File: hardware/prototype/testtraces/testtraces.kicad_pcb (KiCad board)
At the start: 2 copper layers, 0 parts

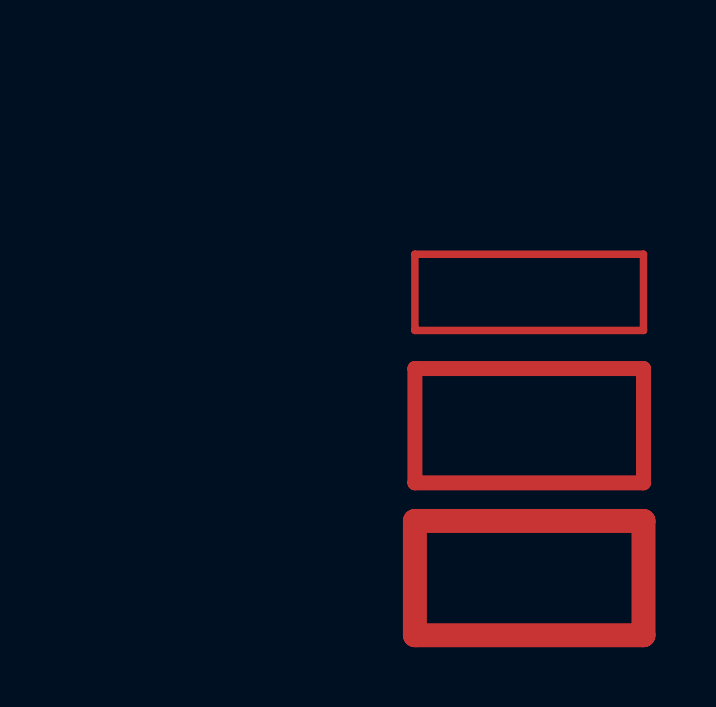
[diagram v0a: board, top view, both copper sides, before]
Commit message: Rerouted pi connect prototype for a slightly smaller board.
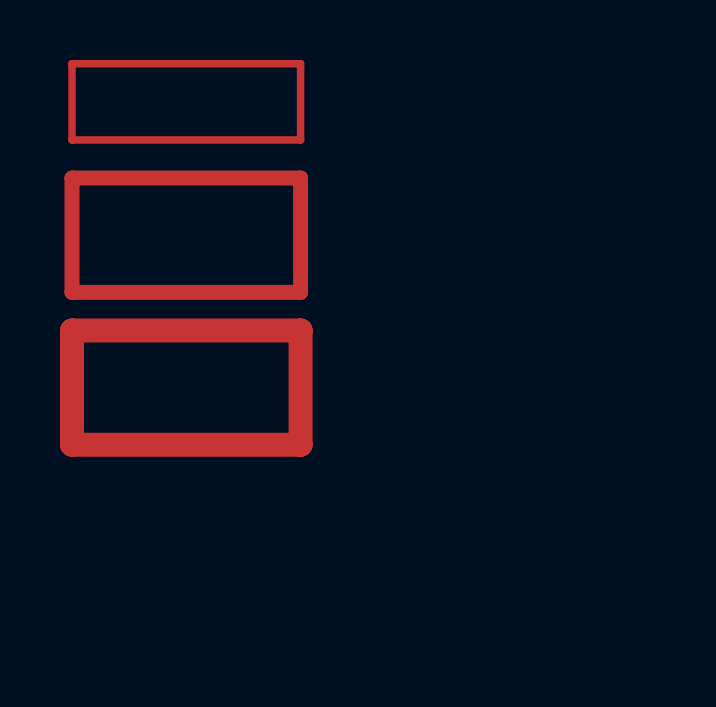
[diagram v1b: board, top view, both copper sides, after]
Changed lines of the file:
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@@
     (uvia_drill 0.1)
   )
-  (gr_text "0.6\n" (at 36.83 29.21) (layer Dwgs.User)
+  (gr_text "0.6\n" (at 25.4 22.86) (layer Dwgs.User)
     (effects (font (size 1.5 1.5) (thickness 0.3)))
   )
-  (gr_text 0.5 (at 36.83 25.4) (layer Dwgs.User)
+  (gr_text 0.5 (at 25.4 19.05) (layer Dwgs.User)
     (effects (font (size 1.5 1.5) (thickness 0.3)))
   )
-  (gr_text 0.25 (at 34.29 20.32) (layer Dwgs.User)
+  (gr_text 0.25 (at 22.86 13.97) (layer Dwgs.User)
     (effects (font (size 1.5 1.5) (thickness 0.3)) (justify left))
   )
-  (segment (start 31.75 21.59) (end 24.13 21.59) (width 0.25) (layer F.Cu) (net 0))
-  (segment (start 31.75 19.05) (end 31.75 21.59) (width 0.25) (layer F.Cu) (net 0))
-  (segment (start 24.13 19.05) (end 31.75 19.05) (width 0.25) (layer F.Cu) (net 0))
-  (segment (start 24.13 21.59) (end 24.13 19.05) (width 0.25) (layer F.Cu) (net 0))
-  (segment (start 24.13 31.75) (end 24.13 27.94) (width 0.8) (layer F.Cu) (net 0))
-  (segment (start 31.75 31.75) (end 24.13 31.75) (width 0.8) (layer F.Cu) (net 0))
-  (segment (start 31.75 27.94) (end 31.75 31.75) (width 0.8) (layer F.Cu) (net 0))
-  (segment (start 24.13 27.94) (end 31.75 27.94) (width 0.8) (layer F.Cu) (net 0))
-  (segment (start 24.13 26.67) (end 24.13 22.86) (width 0.5) (layer F.Cu) (net 0))
-  (segment (start 31.75 26.67) (end 24.13 26.67) (width 0.5) (layer F.Cu) (net 0))
-  (segment (start 31.75 22.86) (end 31.75 26.67) (width 0.5) (layer F.Cu) (net 0))
-  (segment (start 24.13 22.86) (end 31.75 22.86) (width 0.5) (layer F.Cu) (net 0))
+  (segment (start 20.32 15.24) (end 12.7 15.24) (width 0.25) (layer F.Cu) (net 0))
+  (segment (start 20.32 12.7) (end 20.32 15.24) (width 0.25) (layer F.Cu) (net 0))
+  (segment (start 12.7 12.7) (end 20.32 12.7) (width 0.25) (layer F.Cu) (net 0))
+  (segment (start 12.7 15.24) (end 12.7 12.7) (width 0.25) (layer F.Cu) (net 0))
+  (segment (start 12.7 25.4) (end 12.7 21.59) (width 0.8) (layer F.Cu) (net 0))
+  (segment (start 20.32 25.4) (end 12.7 25.4) (width 0.8) (layer F.Cu) (net 0))
+  (segment (start 20.32 21.59) (end 20.32 25.4) (width 0.8) (layer F.Cu) (net 0))
+  (segment (start 12.7 21.59) (end 20.32 21.59) (width 0.8) (layer F.Cu) (net 0))
+  (segment (start 12.7 20.32) (end 12.7 16.51) (width 0.5) (layer F.Cu) (net 0))
+  (segment (start 20.32 20.32) (end 12.7 20.32) (width 0.5) (layer F.Cu) (net 0))
+  (segment (start 20.32 16.51) (end 20.32 20.32) (width 0.5) (layer F.Cu) (net 0))
+  (segment (start 12.7 16.51) (end 20.32 16.51) (width 0.5) (layer F.Cu) (net 0))
 )
